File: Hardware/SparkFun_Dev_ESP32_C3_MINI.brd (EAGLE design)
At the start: 17.8 x 33 mm, 44 parts, among them J1 USB Female Type C Connector, J5 Vertical Qwiic Connector, U1 ESP32-C3_MINI-1, U2 RT9080-33GJ5

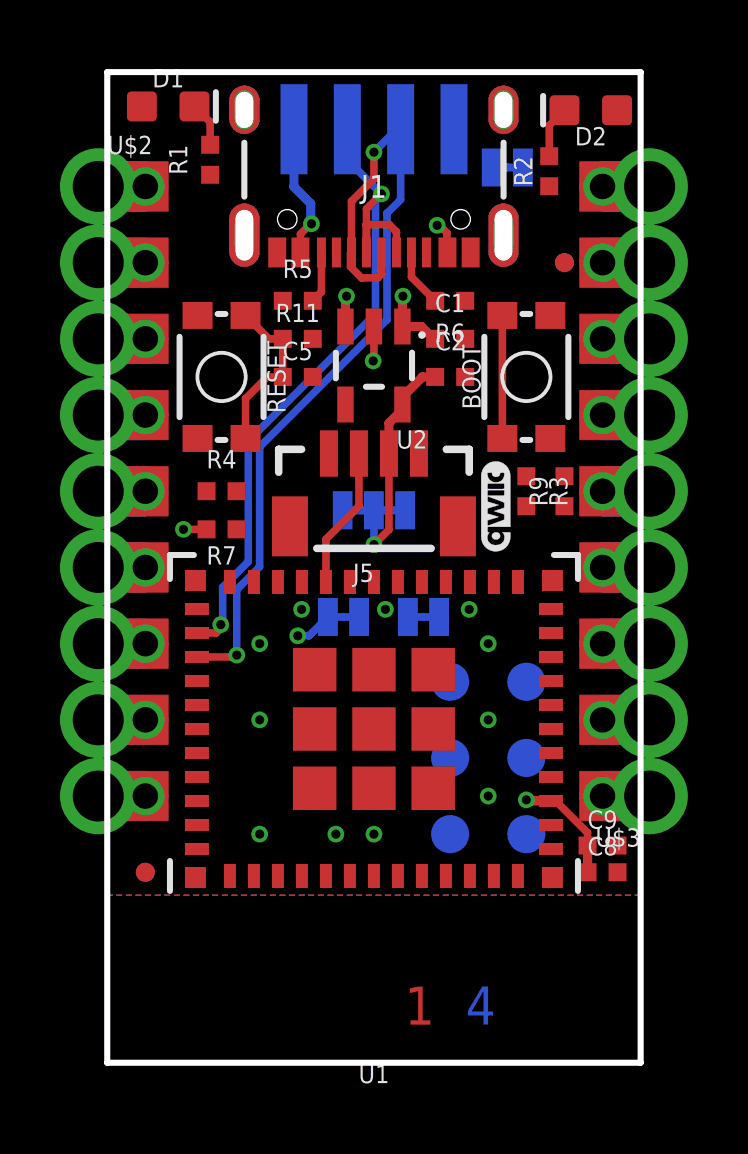
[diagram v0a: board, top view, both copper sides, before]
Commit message: Routes most signals (soppily)
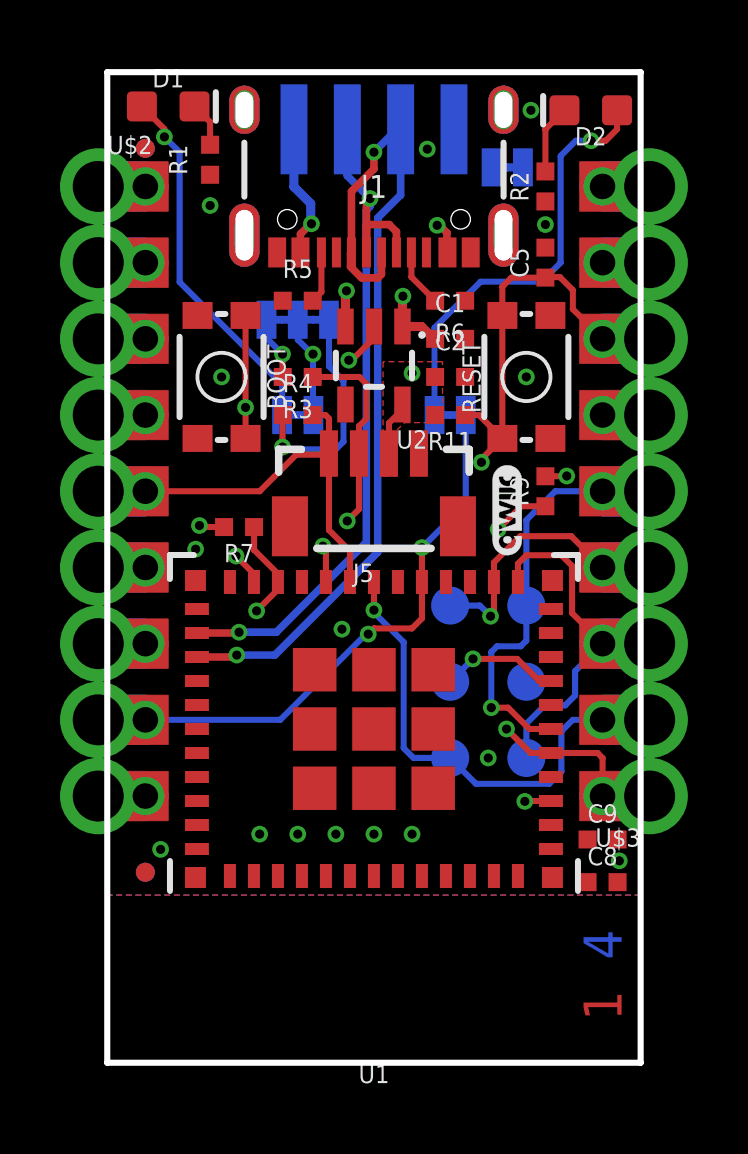
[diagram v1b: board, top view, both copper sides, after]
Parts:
- moved FD1 14.5 mm to (2.54, 30.5)
- moved FD2 14.5 mm to (2.54, 30.5)
- moved BOOT 10.2 mm to (5.08, 22.9), turned to 270 degrees
- moved RESET 10.2 mm to (15.2, 22.9), turned to 90 degrees
- moved C5 9.09 mm to (15.9, 26.7), turned to 90 degrees
- moved R3 8.52 mm to (7.62, 22.9), turned to 180 degrees
- moved PWR 6.90 mm to (7.62, 21.6), turned to 180 degrees
- moved I2C 6.84 mm to (7.62, 24.8), turned to 0 degrees
- moved STAT 6.79 mm to (12.7, 21.6)
- moved R11 5.68 mm to (12.7, 21.6), turned to 180 degrees
- moved R4 3.59 mm to (7.62, 21.6)
- moved TP1 2.54 mm to (15.2, 15.2)
- moved TP6 2.54 mm to (12.7, 15.2)
- moved TP3 2.54 mm to (15.2, 10.2)
- moved TP4 2.54 mm to (12.7, 10.2)
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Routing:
- net IO10/I2S_WS: track 0.00 -> 18.5 mm, vias 0 -> 2
- net EN: track 5.70 -> 23.2 mm, vias 0 -> 2
- net IOA4/MTMS: track 0.00 -> 14.9 mm, vias 0 -> 1
- net N$11: track 0.00 -> 14.5 mm, vias 0 -> 1
- net IOA2: track 0.00 -> 13.5 mm, vias 0 -> 2
- net IO5/SCL/BCK: track 0.00 -> 13.0 mm
- net IO8: track 0.00 -> 12.9 mm, vias 0 -> 1
- net IOA3/PICO/MTDO: track 0.00 -> 12.9 mm, vias 0 -> 1
- net N$2: track 0.00 -> 12.2 mm, vias 0 -> 1
- net IOA0/SCLK/MTCK: track 0.00 -> 11.0 mm
- net IOA1/POCI/MTDI: track 0.00 -> 7.75 mm, vias 0 -> 1
- net N$5: track 0.00 -> 7.50 mm, vias 0 -> 1
- net V_USB: track 8.91 -> 16.1 mm
- net 3.3V: track 14.6 -> 8.01 mm, vias 4 -> 5
- net IO9/BOOT: track 4.10 -> 10.6 mm, vias 0 -> 2
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- added copper zone on layer 1, net 3.3V

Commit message: Routes EVEN MORE signals again, sloppily - no judgements
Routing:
- net IO7/I2S_SDI: track 0.00 -> 8.18 mm, vias 0 -> 1
- net 3.3V: vias 5 -> 6
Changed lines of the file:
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@@
 <vertex x="10.4648" y="23.368"/>
 </polygon>
-<via x="11.43" y="22.987" extent="1-16" drill="0.3048"/>
+<via x="11.5062" y="22.987" extent="1-16" drill="0.3048"/>
 <wire x1="15.875" y1="19.55" x2="16.5782" y2="19.55" width="0.2032" layer="1"/>
 <wire x1="16.5782" y1="19.55" x2="16.5862" y2="19.558" width="0.2032" layer="1"/>
@@
 <wire x1="7.62" y1="24.765" x2="7.62" y2="24.1046" width="0.2032" layer="16"/>
 <wire x1="8.128" y1="23.622" x2="8.1026" y2="23.622" width="0.2032" layer="16"/>
+<via x="10.8204" y="22.987" extent="1-16" drill="0.3048"/>
 <wire x1="17.28" y1="7.4422" x2="17.28" y2="6.0198" width="0" layer="19" extent="1-1"/>
 <wire x1="16.06" y1="8.7252" x2="17.28" y2="7.4422" width="0" layer="19" extent="1-1"/>
@@
 <wire x1="6.96" y1="15.7738" x2="6.2484" y2="15.0622" width="0.2032" layer="1"/>
 <via x="6.2484" y="15.0622" extent="1-16" drill="0.3048"/>
-<wire x1="2.54" y1="8.89" x2="5.08" y2="8.89" width="0.2032" layer="2"/>
-<wire x1="5.08" y1="8.89" x2="6.2484" y2="10.0584" width="0.2032" layer="2"/>
-<wire x1="6.2484" y1="10.0584" x2="6.2484" y2="15.0622" width="0.2032" layer="2"/>
+<wire x1="2.54" y1="8.89" x2="5.08" y2="8.89" width="0.2032" layer="15"/>
+<wire x1="5.08" y1="8.89" x2="6.2484" y2="10.0584" width="0.2032" layer="15"/>
+<wire x1="6.2484" y1="10.0584" x2="6.2484" y2="15.0622" width="0.2032" layer="15"/>
 <wire x1="0.97" y1="8.89" x2="2.54" y2="8.89" width="0" layer="19" extent="1-1"/>
 </signal>
@@
 <wire x1="5.88" y1="20.81" x2="5.88" y2="21.844" width="0.2032" layer="1"/>
 <via x="5.88" y="21.844" extent="1-16" drill="0.3048"/>
-<wire x1="5.88" y1="21.844" x2="5.88" y2="17.2084" width="0.2032" layer="2"/>
-<wire x1="5.88" y1="17.2084" x2="5.5626" y2="16.891" width="0.2032" layer="2"/>
+<wire x1="5.88" y1="21.844" x2="5.88" y2="17.2084" width="0.2032" layer="15"/>
+<wire x1="5.88" y1="17.2084" x2="5.5626" y2="16.891" width="0.2032" layer="15"/>
 <via x="5.5626" y="16.891" extent="1-16" drill="0.3048"/>
 <wire x1="6.16" y1="16.0252" x2="6.16" y2="16.2936" width="0.2032" layer="1"/>
@@
 <contactref element="U$2" pad="3"/>
 <contactref element="U1" pad="21"/>
-<wire x1="2.54" y1="13.97" x2="7.76" y2="16.0252" width="0" layer="19" extent="1-1"/>
+<wire x1="7.76" y1="16.0252" x2="7.76" y2="15.7864" width="0.2032" layer="1"/>
+<wire x1="6.858" y1="14.8844" x2="6.858" y2="12.954" width="0.2032" layer="1"/>
+<via x="6.858" y="12.954" extent="1-16" drill="0.3048"/>
+<wire x1="7.76" y1="15.7864" x2="6.858" y2="14.8844" width="0.2032" layer="1"/>
+<wire x1="6.858" y1="12.954" x2="3.556" y2="12.954" width="0.2032" layer="2"/>
+<wire x1="3.556" y1="12.954" x2="2.54" y2="13.97" width="0.2032" layer="2"/>
 <wire x1="0.97" y1="13.97" x2="2.54" y2="13.97" width="0" layer="19" extent="1-1"/>
 </signal>

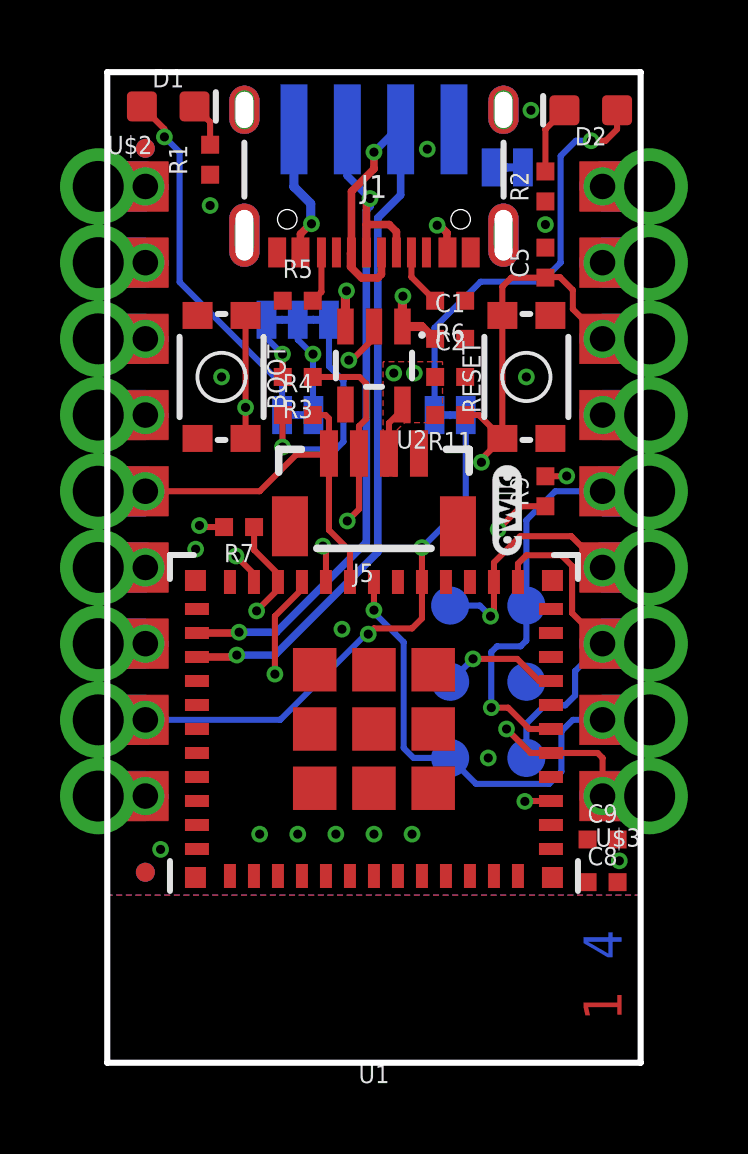
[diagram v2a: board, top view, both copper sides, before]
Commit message: Slight adjustment to TX
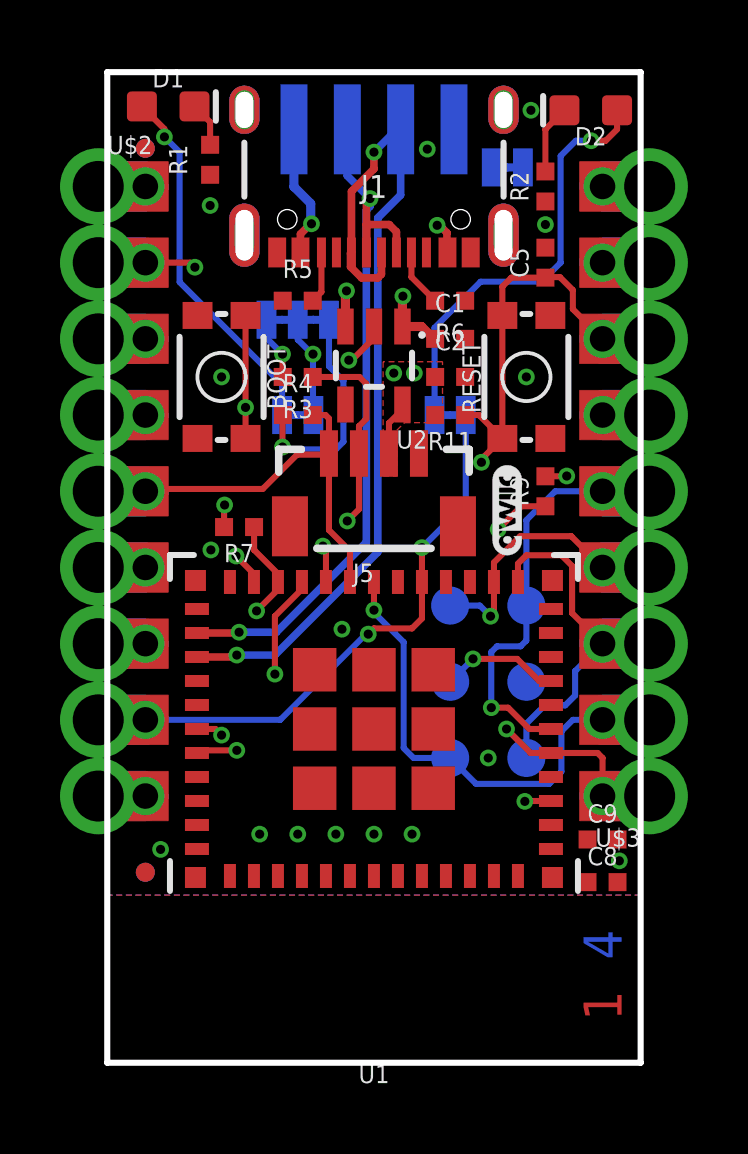
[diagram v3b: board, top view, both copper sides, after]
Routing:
- net IO20/TXO: track 0.00 -> 20.3 mm, vias 0 -> 1
- net IO21/RXI: track 0.00 -> 19.8 mm, vias 0 -> 2
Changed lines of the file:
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@@
 <wire x1="16.5782" y1="19.55" x2="16.5862" y2="19.558" width="0.2032" layer="1"/>
 <via x="16.5862" y="19.558" extent="1-16" drill="0.3048"/>
-<wire x1="5.1642" y1="17.8562" x2="4.3942" y2="17.8562" width="0.2032" layer="1"/>
-<wire x1="4.3942" y1="17.8562" x2="4.3434" y2="17.907" width="0.2032" layer="1"/>
-<via x="4.3434" y="17.907" extent="1-16" drill="0.3048"/>
+<wire x1="5.1816" y1="18.5928" x2="5.1642" y2="18.5754" width="0.2032" layer="1"/>
+<wire x1="5.1642" y1="17.8562" x2="5.1642" y2="18.5754" width="0.2032" layer="1"/>
+<via x="5.1816" y="18.5928" extent="1-16" drill="0.3048"/>
 <wire x1="16.06" y1="8.7252" x2="15.2022" y2="8.7252" width="0.2032" layer="1"/>
 <wire x1="15.2022" y1="8.7252" x2="15.1892" y2="8.7122" width="0.2032" layer="1"/>
@@
 <wire x1="9.4234" y1="23.4188" x2="9.3218" y2="23.4188" width="0.2032" layer="1"/>
 <via x="9.3218" y="23.4188" extent="1-16" drill="0.3048"/>
-<via x="4.2164" y="17.1196" extent="1-16" drill="0.3048"/>
+<via x="4.7244" y="17.0942" extent="1-16" drill="0.3048"/>
 <via x="5.08" y="22.86" extent="1-16" drill="0.3048"/>
 <via x="15.24" y="22.86" extent="1-16" drill="0.3048"/>
@@
 <contactref element="U$2" pad="8"/>
 <contactref element="U1" pad="31"/>
-<wire x1="0.97" y1="26.67" x2="2.54" y2="26.67" width="0" layer="19" extent="1-1"/>
-<wire x1="4.26" y1="10.3252" x2="2.54" y2="26.67" width="0" layer="19" extent="1-1"/>
+<wire x1="4.26" y1="10.3252" x2="4.3488" y2="10.414" width="0.2032" layer="1"/>
+<wire x1="4.3488" y1="10.414" x2="5.588" y2="10.414" width="0.2032" layer="1"/>
+<via x="5.588" y="10.414" extent="1-16" drill="0.3048"/>
+<wire x1="5.588" y1="10.414" x2="5.588" y2="12.6746" width="0.2032" layer="15"/>
+<wire x1="4.191" y1="14.0716" x2="4.191" y2="26.5176" width="0.2032" layer="15"/>
+<via x="4.191" y="26.5176" extent="1-16" drill="0.3048"/>
+<wire x1="5.588" y1="12.6746" x2="4.191" y2="14.0716" width="0.2032" layer="15"/>
+<wire x1="2.54" y1="26.67" x2="4.0386" y2="26.67" width="0.2032" layer="1"/>
+<wire x1="4.0386" y1="26.67" x2="4.191" y2="26.5176" width="0.2032" layer="1"/>
+<wire x1="2.54" y1="26.67" x2="0.97" y2="26.67" width="0" layer="19" extent="1-1"/>
 </signal>
 <signal name="IO20/TXO">
@@
 <contactref element="U$2" pad="9"/>
 <contactref element="U1" pad="30"/>
-<wire x1="0.97" y1="29.21" x2="2.54" y2="29.21" width="0" layer="19" extent="1-1"/>
-<wire x1="4.26" y1="11.1252" x2="2.54" y2="29.21" width="0" layer="19" extent="1-1"/>
+<wire x1="4.26" y1="11.1252" x2="4.8768" y2="11.1252" width="0.2032" layer="1"/>
+<wire x1="4.8768" y1="11.1252" x2="5.08" y2="10.922" width="0.2032" layer="1"/>
+<via x="5.08" y="10.922" extent="1-16" drill="0.3048"/>
+<wire x1="3.7084" y1="28.0416" x2="2.54" y2="29.21" width="0.2032" layer="15"/>
+<wire x1="5.08" y1="10.922" x2="5.0292" y2="10.922" width="0.2032" layer="15"/>
+<wire x1="5.0292" y1="10.922" x2="3.7084" y2="12.2428" width="0.2032" layer="15"/>
+<wire x1="3.7084" y1="12.2428" x2="3.7084" y2="28.0416" width="0.2032" layer="15"/>
+<wire x1="2.54" y1="29.21" x2="0.97" y2="29.21" width="0" layer="19" extent="1-1"/>
 </signal>
 <signal name="IOA2">
@@
 <wire x1="8.66" y1="17.756" x2="9.36" y2="17.056" width="0.2032" layer="1"/>
 <wire x1="8.66" y1="20.307" x2="8.66" y2="17.756" width="0.2032" layer="1"/>
-<wire x1="6.35" y1="19.05" x2="2.54" y2="19.05" width="0.2032" layer="1"/>
+<wire x1="6.4516" y1="19.1262" x2="2.6162" y2="19.1262" width="0.2032" layer="1"/>
+<wire x1="2.6162" y1="19.1262" x2="2.54" y2="19.05" width="0.2032" layer="1"/>
 <wire x1="8.12" y1="21.59" x2="8.1708" y2="21.6408" width="0.2032" layer="1"/>
 <wire x1="8.6614" y1="20.3084" x2="8.66" y2="20.307" width="0.2032" layer="1"/>
 <wire x1="8.6222" y1="20.2692" x2="8.66" y2="20.307" width="0.2032" layer="1"/>
-<wire x1="6.35" y1="19.05" x2="7.5692" y2="20.2692" width="0.2032" layer="1"/>
-<wire x1="7.5692" y1="20.2692" x2="8.6222" y2="20.2692" width="0.2032" layer="1"/>
+<wire x1="6.4516" y1="19.1262" x2="7.5946" y2="20.2692" width="0.2032" layer="1"/>
+<wire x1="7.5946" y1="20.2692" x2="8.6222" y2="20.2692" width="0.2032" layer="1"/>
 <wire x1="8.66" y1="20.307" x2="8.66" y2="21.4754" width="0.2032" layer="1"/>
 <wire x1="8.12" y1="21.59" x2="8.5454" y2="21.59" width="0.2032" layer="1"/>
@@
 <via x="6.858" y="12.954" extent="1-16" drill="0.3048"/>
 <wire x1="7.76" y1="15.7864" x2="6.858" y2="14.8844" width="0.2032" layer="1"/>
-<wire x1="6.858" y1="12.954" x2="3.556" y2="12.954" width="0.2032" layer="2"/>
-<wire x1="3.556" y1="12.954" x2="2.54" y2="13.97" width="0.2032" layer="2"/>
+<wire x1="6.858" y1="12.954" x2="6.6548" y2="12.7508" width="0.2032" layer="2"/>
+<wire x1="6.6548" y1="12.7508" x2="3.7592" y2="12.7508" width="0.2032" layer="2"/>
+<wire x1="3.7592" y1="12.7508" x2="2.54" y2="13.97" width="0.2032" layer="2"/>
 <wire x1="0.97" y1="13.97" x2="2.54" y2="13.97" width="0" layer="19" extent="1-1"/>
 </signal>
